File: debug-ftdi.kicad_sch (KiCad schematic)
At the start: 74 parts, among them J3 USB-C_GCT_USB4105-GF-A, U13 TXU0304BQAR, U32 TXS0102DQER, U33 TXS0102DQER, U5 NCP718BSN330T1G, U6 FT4232H_VQFN, U7 TXU0304BQAR, U8 TPD4E05U06QDQARQ1, U9 SN74HC595B, Y1 Resonator_12MHz_ABM8G

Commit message: [#65754] Rename project
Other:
- title: SO-DIMM DDR5 Tester -> RDIMM DDR5 Tester

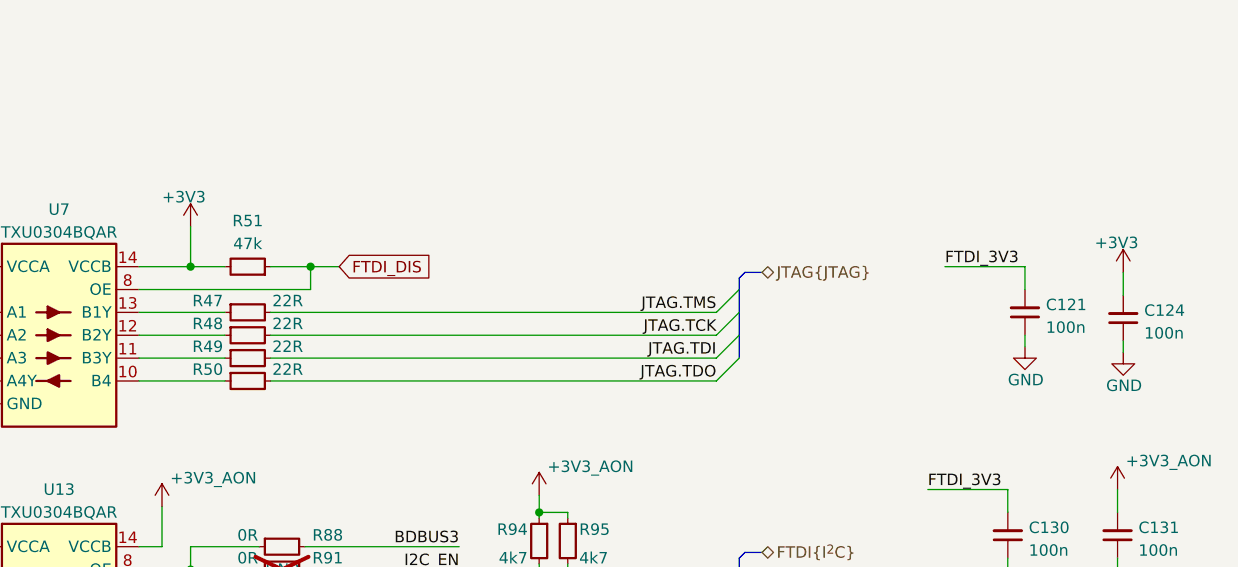
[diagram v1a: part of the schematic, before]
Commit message: [#66727] Change FTDI JTAG voltage level to 1V8
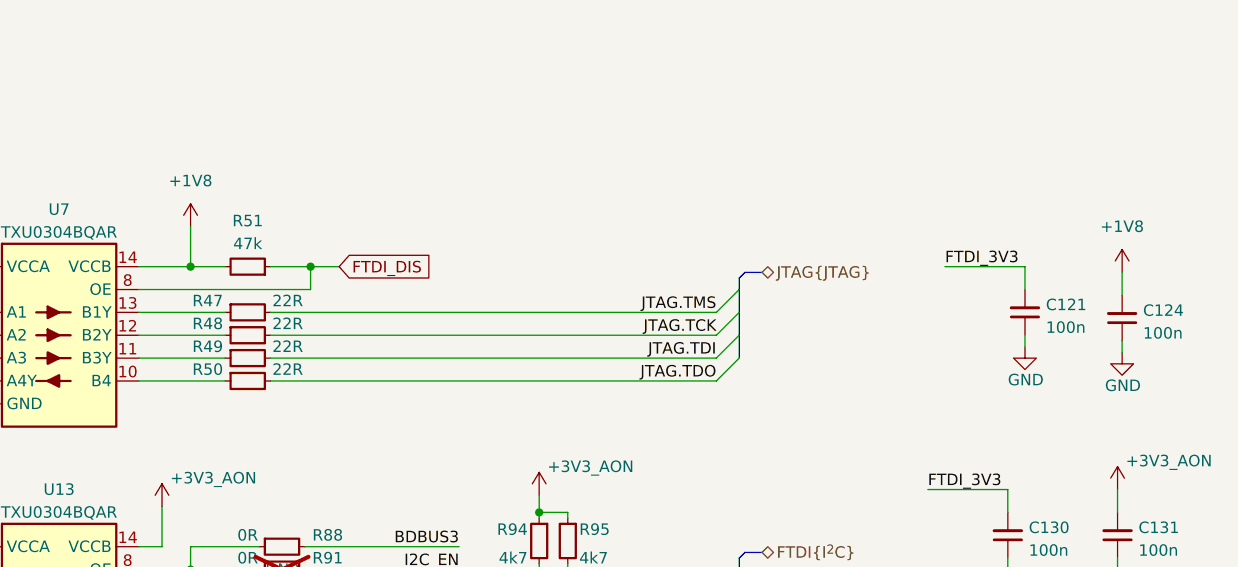
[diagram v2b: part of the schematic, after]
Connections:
- net +3V3: no longer C124.2, R51.2, U7.14 (VCCB)
- new net +1V8: C124.2, R51.2, U7.14 (VCCB)

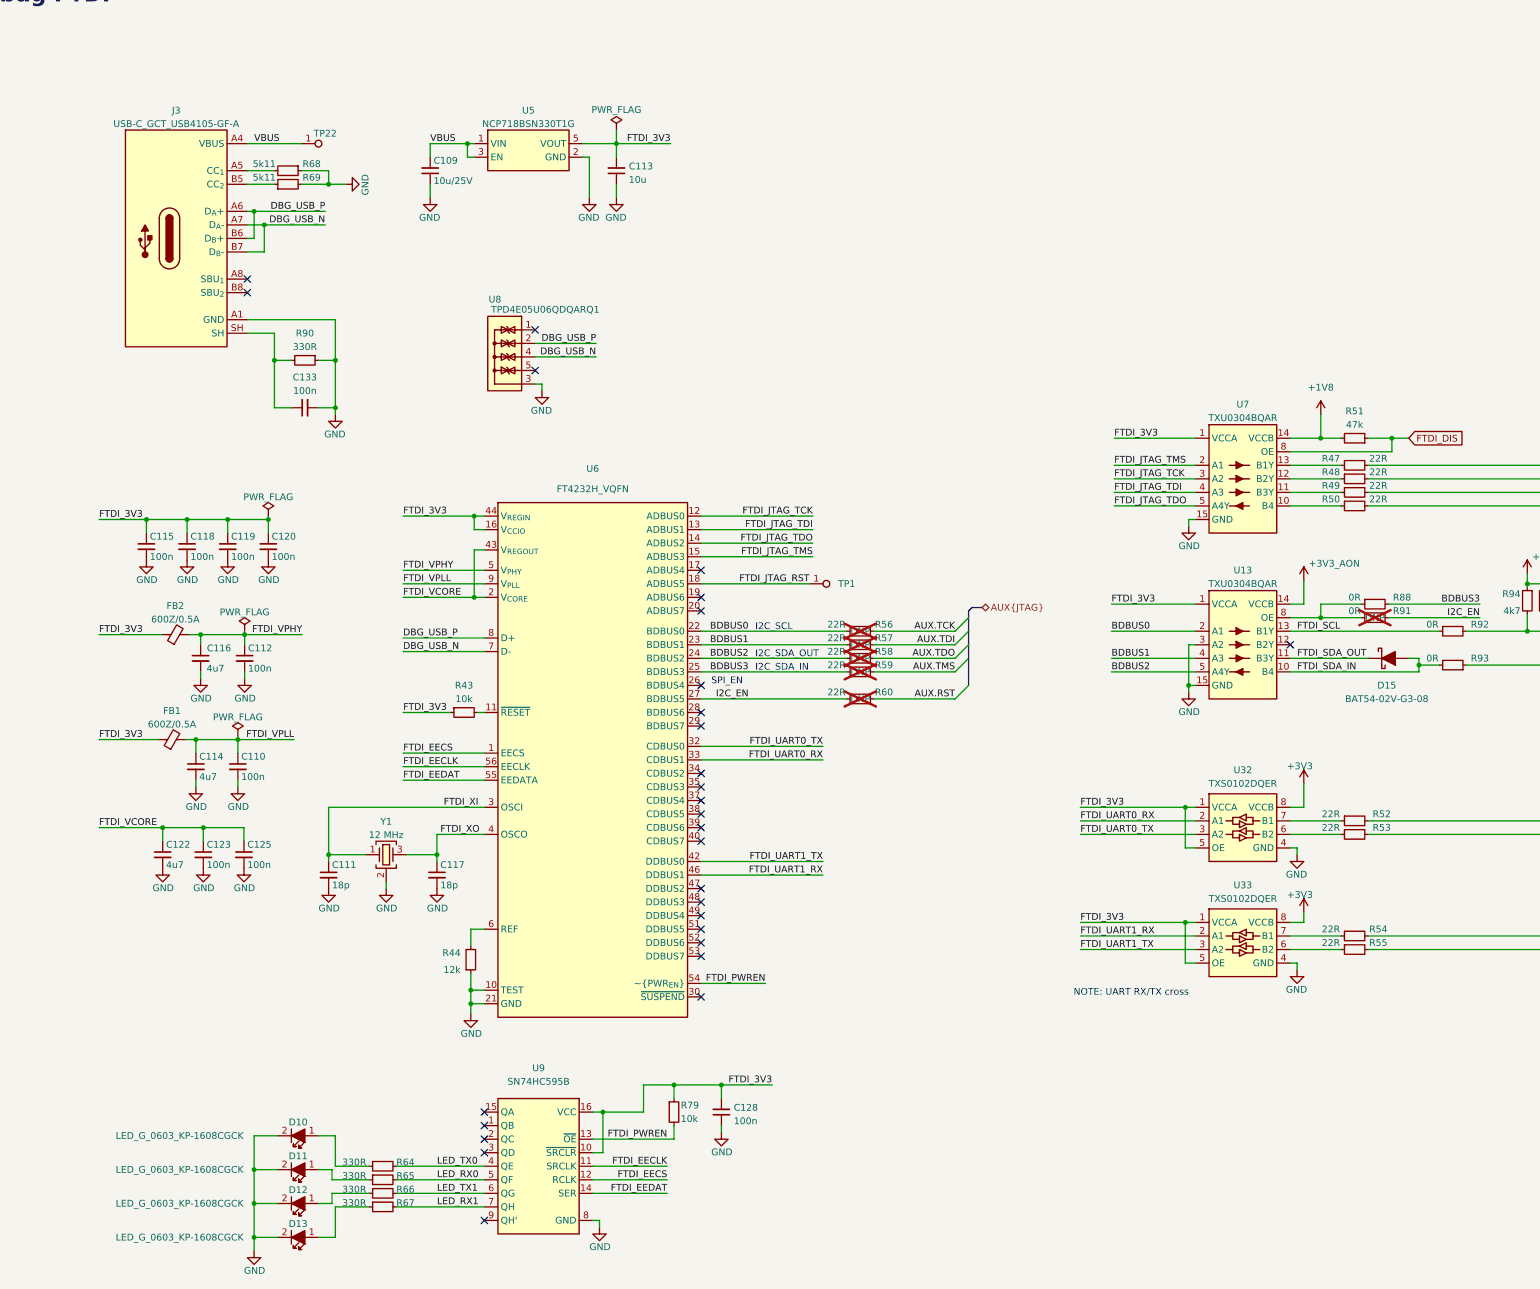
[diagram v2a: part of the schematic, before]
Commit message: [#67725] Update debug ftdi
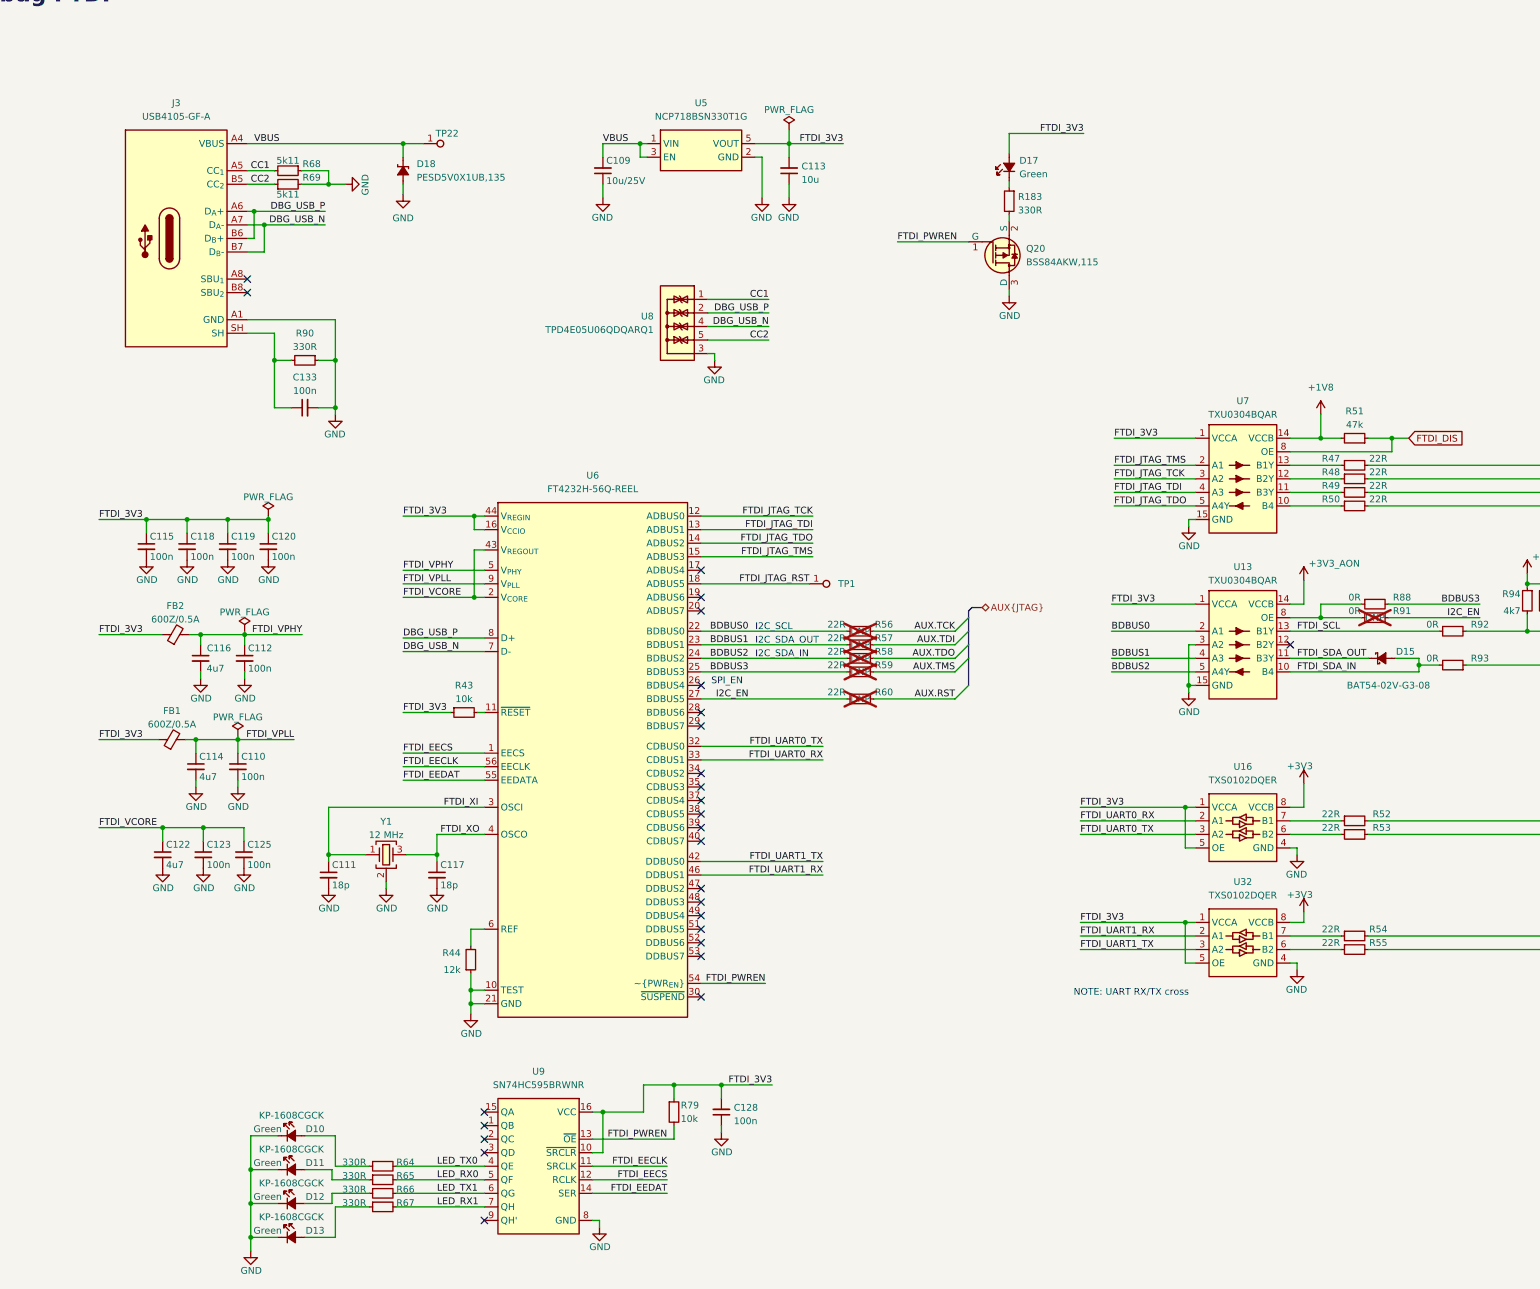
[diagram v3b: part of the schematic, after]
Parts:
- removed U33: TXS0102DQER, antmicro-footprints:X2SON8_1.4x1x0.32mm_P0.35mm, symbol antmicroLogicTranslatorsLevelShifters:TXS0102DQER
- added D17: LED_G_0402_VLMTG1500-GS08, antmicro-footprints:LED_0402_1005Metric_G, symbol antmicroLEDIndicationDiscrete:LED_G_0402_VLMTG1500-GS08
- added D18: PESD5V0X1UB, antmicro-footprints:SOD-523, symbol antmicroTVSDiodes:PESD5V0X1UB
- added Q20: BSS84AKW, antmicro-footprints:SOT-323, symbol antmicroTransistorsFETsMOSFETsSingle:BSS84AKW
- added R183: R_330R_0402, antmicro-footprints:R_0402_1005Metric, symbol antmicroResistors0402:R_330R_0402
- added U16: TXS0102DQER, antmicro-footprints:X2SON8_1.4x1x0.32mm_P0.35mm, symbol antmicroLogicTranslatorsLevelShifters:TXS0102DQER
- D10, D11, D12, D13: Color (none) -> Green
- J3: VSD_Class USB-C -> (none)
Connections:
- net +3V3: now also U16.8 (VCCB)
- net FTDI_3V3: now also D17.2 (A), U16.1 (VCCA), U16.5 (OE)
- net FTDI_PWREN: now also Q20.1 (G)
- net FTDI_UART0_RX: now also U16.2 (A1); no longer U32.2 (A1)
- net FTDI_UART0_TX: now also U16.3 (A2); no longer U32.3 (A2)
- net FTDI_UART1_RX: now also U32.2 (A1)
- net FTDI_UART1_TX: now also U32.3 (A2)
- net GND: now also D10.1 (C), D11.1 (C), D12.1 (C), D13.1 (C), D18.2 (A), Q20.3 (D), U16.4 (GND); no longer D10.2, D11.2, D12.2, D13.2
- net VBUS: now also D18.1 (C)
- net at R52.1: now also U16.7 (B1); no longer U32.7 (B1)
- net at R55.1: now also U32.6 (B2)
- net at R53.1: now also U16.6 (B2); no longer U32.6 (B2)
- net at R54.1: now also U32.7 (B1)
- net CC1: now reaches J3.A5 (CC_{1}), R68.2
- net CC1: now also U8.1, U8.10
- net CC2: now reaches J3.B5 (CC_{2}), R69.1
- net CC2: now also U8.5, U8.6
- net at R65.1: now also D11.2 (A); no longer D11.1
- net at R66.1: now also D12.2 (A); no longer D12.1
- net at R67.1: now also D13.2 (A); no longer D13.1
- net at R64.1: now also D10.2 (A); no longer D10.1
- new net: D17.1 (C), R183.1
- new net: Q20.2 (S), R183.2
- no-connect marks 29 -> 27
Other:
- moved on the sheet: C109, C113, TP22

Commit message: [#67725] Add VNA calibration circuits
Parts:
- added J13, J14, J15, J16, J9: U_FL-R-SMT-1, antmicro-footprints:Coax_Conn_U.FL, symbol antmicroCoaxialConnectorsRF:U_FL-R-SMT-1
- added R233: R_49R9_0402, antmicro-footprints:R_0402_1005Metric, symbol antmicroResistors0402:R_49R9_0402
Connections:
- net GND: now also J13.1, J13.SH1, J13.SH2, J14.SH1, J14.SH2, J15.SH1, J15.SH2, J16.SH1, J16.SH2, J9.SH1, J9.SH2, R233.1
- new net: J14.1, R233.2
- new net: J15.1, J16.1
- no-connect marks 27 -> 28
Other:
- note added: "50 ohm"
- note added: "LDO"
- note added: "Logic level translators"
- note added: "Open"
- note added: "Pass"
- note added: "Shift register"
- note added: "Short"
- note added: "USB-C"
- note added: "VNA calibration"
- moved on the sheet: C109, C110, C111, C112, C113, C114, C115, C116, C117, C118, C119, C120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

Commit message: [#68016] Clean-up the schematic
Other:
- note added: "FTDI"
- moved on the sheet: C110, C112, C113, C114, C115, C118, C119, C120, C122, C123, C124, C125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
